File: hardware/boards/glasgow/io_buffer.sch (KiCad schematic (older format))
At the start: 66 parts, among them J2 Conn_02x10_Odd_Even, J6 Conn_01x08, J7 Conn_01x08, U10 DAC081C081CIMK, U11 TPS73101DBV, U16 SN74LVC1T45DCKR, U17 SN74LVC1T45DCKR, U18 SN74LVC1T45DCKR, U19 PCA6408APW, U19 SN74LVC1T45DCKR, U20 SN74LVC1T45DCKR, U21 INA233, U21 SN74LVC1T45DCKR, U5 SN74LVC1T45DCKR, U6 SN74LVC1T45DCKR

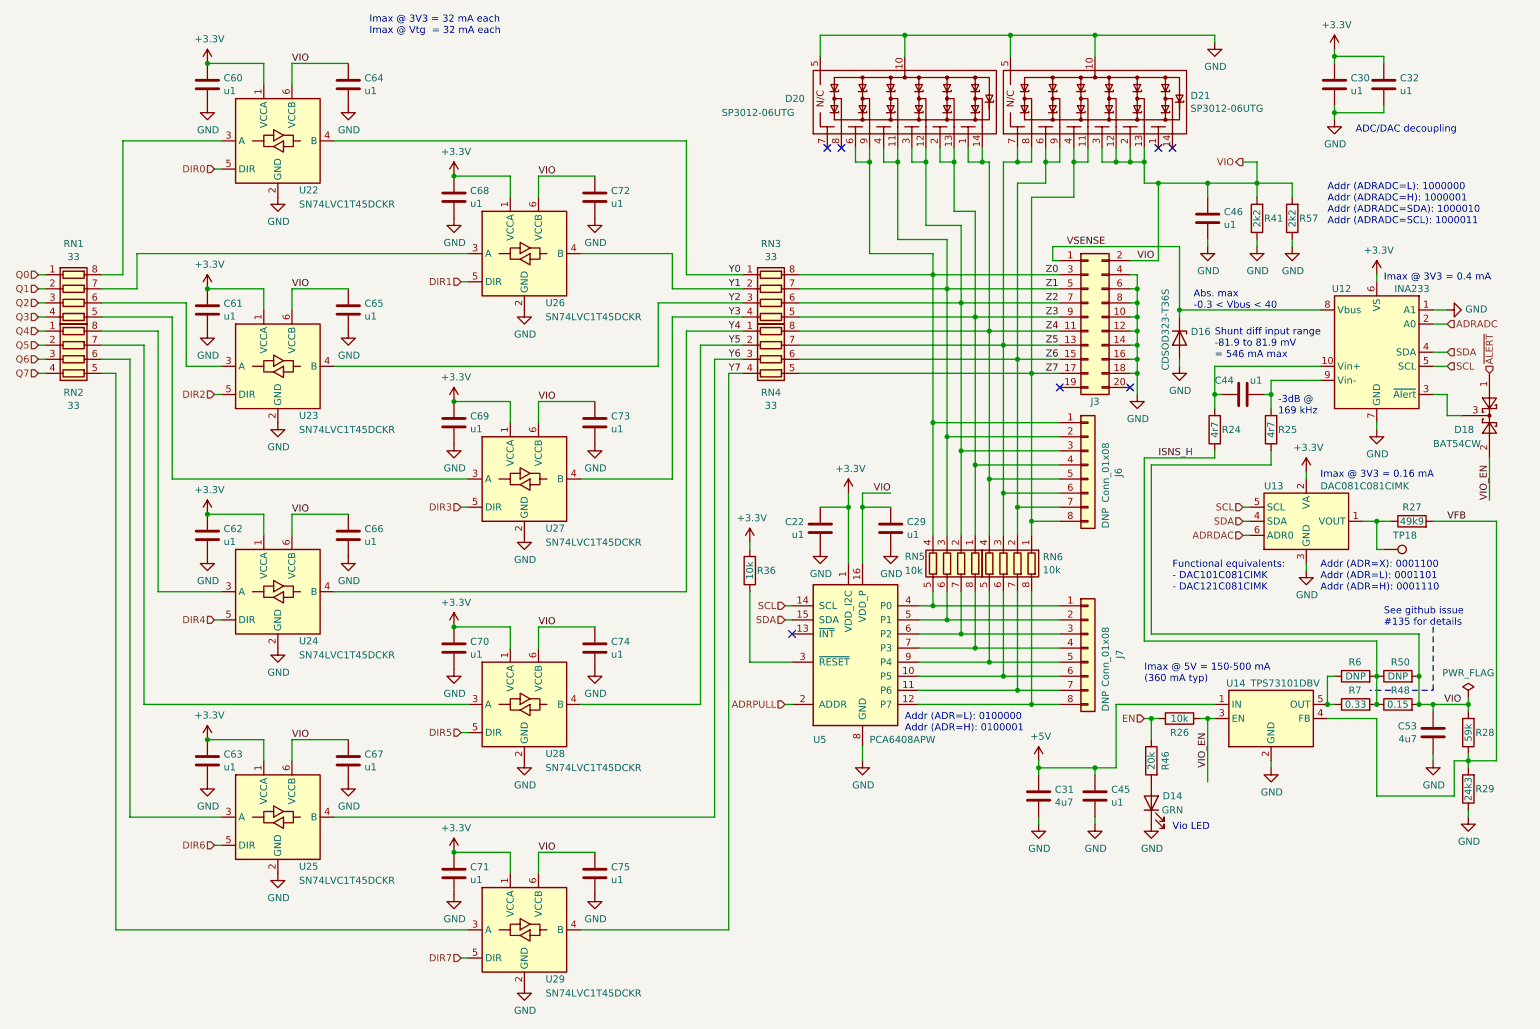
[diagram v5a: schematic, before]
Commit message: revC2: Consolidated sub 1k resistor value notation.
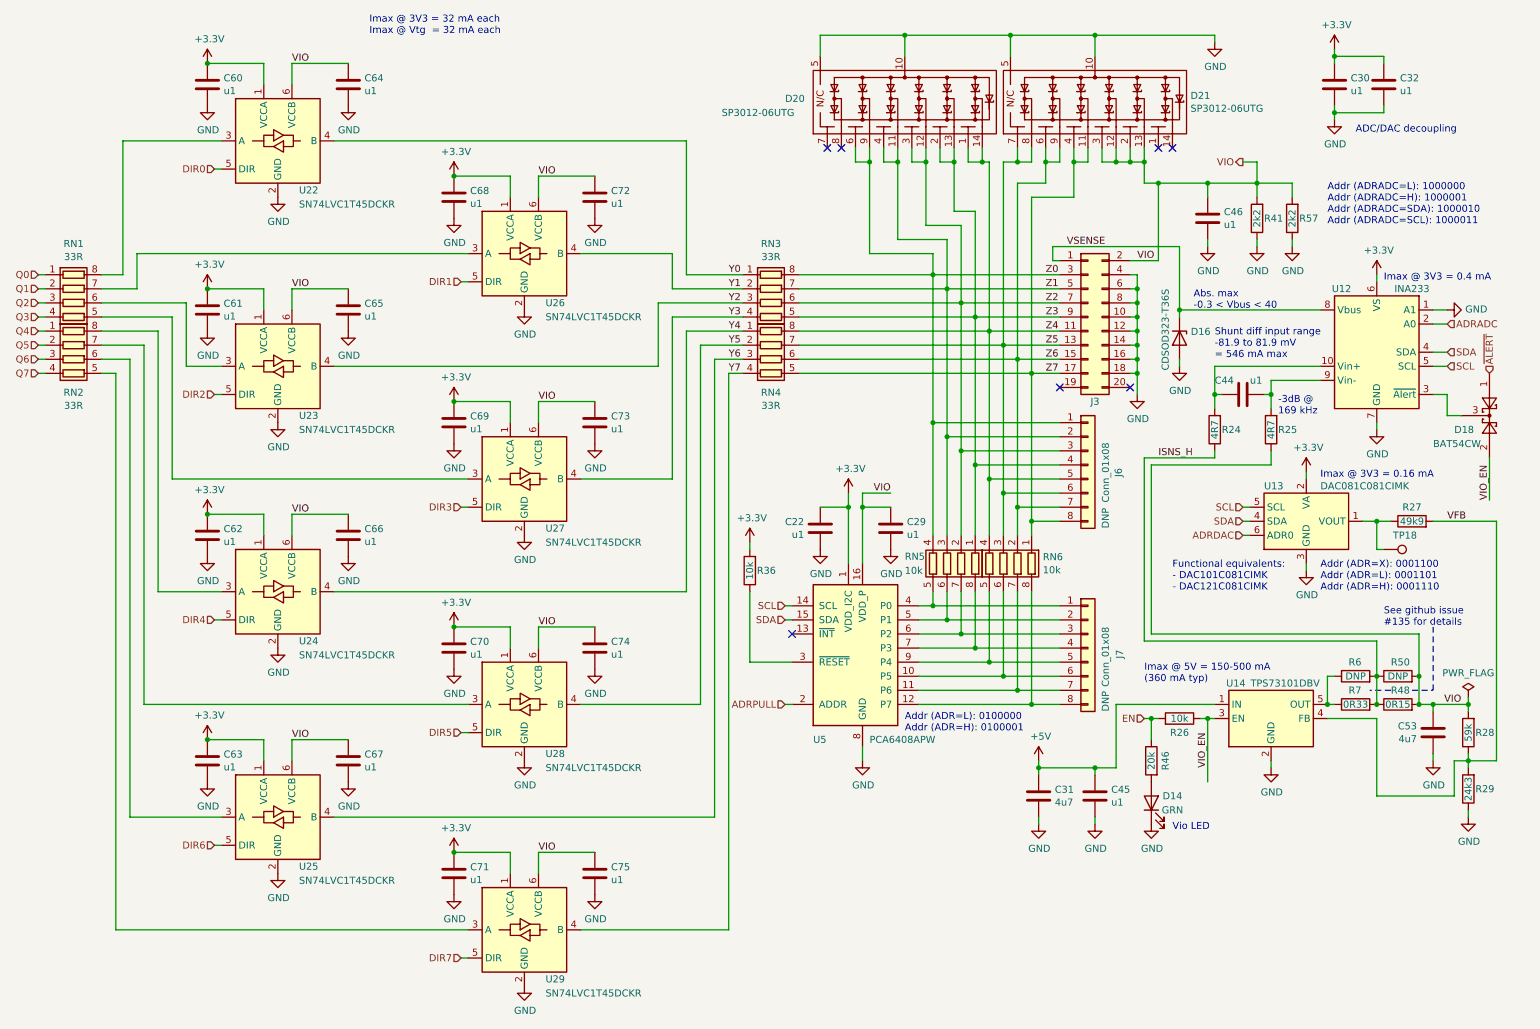
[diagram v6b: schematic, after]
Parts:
- D22, D23: MPN (none) -> SP3012-06UTG; Mfg (none) -> Littlefuse
- R30, R54: value 4r7 -> 4R7; 1b2-bom-key res-0402-4R7 -> res-0402-4r7
- R49: value 0.15 -> 0R15; 1b2-bom-key res-0603-0_15 -> res-0603-0r15
- R56: value 0.33 -> 0R33; 1b2-bom-key res-0603-0_33 -> res-0603-0r33
- RN1, RN2, RN3, RN4: value 33 -> 33R; 1b2-bom-key res-0402cv-array-4-33 -> res-0402cv-array-4-33r; MPN (none) -> YC124-JR-1333RL; Mfg (none) -> Yageo
- RN5, RN6: MPN (none) -> YC124-JR-0710KL; Mfg (none) -> Yageo
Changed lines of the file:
@@
 AR Path="/5C7B59B0/5C9E338E/5CD0C19C" Ref="R48"  Part="1"
 F 0 "R48" V 10550 5500 50  0000 R CNN
-F 1 "0.15" V 10450 5450 50  0000 C CNN
+F 1 "0R15" V 10450 5450 50  0000 C CNN
 F 2 "Resistor_SMD:R_0603_1608Metric" V 10380 5450 50  0001 C CNN
 F 3 "https://www.ohmite.com/assets/docs/res_kdv.pdf" H 10450 5450 50  0001 C CNN
 F 4 "Ohmite" H 4300 500 50  0001 C CNN "Mfg"
 F 5 "KDV06FR150ET" H 4300 500 50  0001 C CNN "MPN"
-F 6 "res-0603-0_15" H 10450 5450 50  0001 C CNN "1b2-bom-key"
+F 6 "res-0603-0r15" H 10450 5450 50  0001 C CNN "1b2-bom-key"
 	1    10450 5450
 	0    -1   -1   0
@@
 AR Path="/5C7B59B0/5C9E337E/5EAC6F23" Ref="RN7"  Part="1"
 F 0 "RN1" V 630 2600 50  0000 C CNN
-F 1 "33" V 723 2600 50  0000 C CNN
+F 1 "33R" V 723 2600 50  0000 C CNN
 F 2 "Glasgow:R_Array_Convex_4x0402" V 1325 2600 50  0001 C CNN
-F 3 "~" H 1050 2600 50  0001 C CNN
-F 4 "res-0402cv-array-4-33" H 1050 2600 50  0001 C CNN "1b2-bom-key"
+F 3 "https://www.mouser.com/datasheet/2/447/PYu-YC_TC_group_51_RoHS_L_7-1313905.pdf" H 1050 2600 50  0001 C CNN
+F 4 "res-0402cv-array-4-33r" H 1050 2600 50  0001 C CNN "1b2-bom-key"
+F 5 "YC124-JR-1333RL" H 1050 2600 50  0001 C CNN "MPN"
+F 6 "Yageo" H 1050 2600 50  0001 C CNN "Mfg"
 	1    1050 2600
 	0    1    1    0
@@
 AR Path="/5C7B59B0/5C9E337E/5EAFC4A6" Ref="RN8"  Part="1"
 F 0 "RN2" V 1286 3000 50  0000 C CNN
-F 1 "33" V 1379 3000 50  0000 C CNN
+F 1 "33R" V 1379 3000 50  0000 C CNN
 F 2 "Glasgow:R_Array_Convex_4x0402" V 1325 3000 50  0001 C CNN
-F 3 "~" H 1050 3000 50  0001 C CNN
-F 4 "res-0402cv-array-4-33" H 1050 3000 50  0001 C CNN "1b2-bom-key"
+F 3 "https://www.mouser.com/datasheet/2/447/PYu-YC_TC_group_51_RoHS_L_7-1313905.pdf" H 1050 3000 50  0001 C CNN
+F 4 "res-0402cv-array-4-33r" H 1050 3000 50  0001 C CNN "1b2-bom-key"
+F 5 "YC124-JR-1333RL" H 1050 3000 50  0001 C CNN "MPN"
+F 6 "Yageo" H 1050 3000 50  0001 C CNN "Mfg"
 	1    1050 3000
 	0    1    1    0
@@
 AR Path="/5C7B59B0/5C9E337E/5EAFCC23" Ref="RN9"  Part="1"
 F 0 "RN3" V 5580 2600 50  0000 C CNN
-F 1 "33" V 5673 2600 50  0000 C CNN
+F 1 "33R" V 5673 2600 50  0000 C CNN
 F 2 "Glasgow:R_Array_Convex_4x0402" V 6275 2600 50  0001 C CNN
-F 3 "~" H 6000 2600 50  0001 C CNN
-F 4 "res-0402cv-array-4-33" H 6000 2600 50  0001 C CNN "1b2-bom-key"
+F 3 "https://www.mouser.com/datasheet/2/447/PYu-YC_TC_group_51_RoHS_L_7-1313905.pdf" H 6000 2600 50  0001 C CNN
+F 4 "res-0402cv-array-4-33r" H 6000 2600 50  0001 C CNN "1b2-bom-key"
+F 5 "YC124-JR-1333RL" H 6000 2600 50  0001 C CNN "MPN"
+F 6 "Yageo" H 6000 2600 50  0001 C CNN "Mfg"
 	1    6000 2600
 	0    1    1    0
@@
 AR Path="/5C7B59B0/5C9E337E/5EB2C386" Ref="RN10"  Part="1"
 F 0 "RN4" V 6236 3000 50  0000 C CNN
-F 1 "33" V 6329 3000 50  0000 C CNN
+F 1 "33R" V 6329 3000 50  0000 C CNN
 F 2 "Glasgow:R_Array_Convex_4x0402" V 6275 3000 50  0001 C CNN
-F 3 "~" H 6000 3000 50  0001 C CNN
-F 4 "res-0402cv-array-4-33" H 6000 3000 50  0001 C CNN "1b2-bom-key"
+F 3 "https://www.mouser.com/datasheet/2/447/PYu-YC_TC_group_51_RoHS_L_7-1313905.pdf" H 6000 3000 50  0001 C CNN
+F 4 "res-0402cv-array-4-33r" H 6000 3000 50  0001 C CNN "1b2-bom-key"
+F 5 "YC124-JR-1333RL" H 6000 3000 50  0001 C CNN "MPN"
+F 6 "Yageo" H 6000 3000 50  0001 C CNN "Mfg"
 	1    6000 3000
 	0    1    1    0
@@
 F 1 "10k" H 7370 4496 50  0000 R CNN
 F 2 "Glasgow:R_Array_Convex_4x0402" V 7925 4450 50  0001 C CNN
-F 3 "~" H 7650 4450 50  0001 C CNN
+F 3 "https://www.mouser.com/datasheet/2/447/PYu-YC_TC_group_51_RoHS_L_7-1313905.pdf" H 7650 4450 50  0001 C CNN
 F 4 "res-0402cv-array-4-10k" H 7650 4450 50  0001 C CNN "1b2-bom-key"
+F 5 "YC124-JR-0710KL" H 7650 4450 50  0001 C CNN "MPN"
+F 6 "Yageo" H 7650 4450 50  0001 C CNN "Mfg"
 	1    7650 4450
 	-1   0    0    1
@@
 F 1 "10k" H 7550 4500 50  0000 R CNN
 F 2 "Glasgow:R_Array_Convex_4x0402" V 7525 4450 50  0001 C CNN
-F 3 "~" H 7250 4450 50  0001 C CNN
+F 3 "https://www.mouser.com/datasheet/2/447/PYu-YC_TC_group_51_RoHS_L_7-1313905.pdf" H 7250 4450 50  0001 C CNN
 F 4 "res-0402cv-array-4-10k" H 7250 4450 50  0001 C CNN "1b2-bom-key"
+F 5 "YC124-JR-0710KL" H 7250 4450 50  0001 C CNN "MPN"
+F 6 "Yageo" H 7250 4450 50  0001 C CNN "Mfg"
 	1    7250 4450
 	-1   0    0    1
@@
 AR Path="/5C7B59B0/5C9E338E/5F1A23B9" Ref="R25"  Part="1"
 F 0 "R25" H 9500 3500 50  0000 R CNN
-F 1 "4r7" V 9550 3500 50  0000 C CNN
+F 1 "4R7" V 9550 3500 50  0000 C CNN
 F 2 "Resistor_SMD:R_0402_1005Metric" V 9480 3500 50  0001 C CNN
 F 3 "https://www.mouser.com/datasheet/2/447/PYu-RC_Group_51_RoHS_L_10-1527934.pdf" H 9550 3500 50  0001 C CNN
 F 4 "Yageo" H 3400 -1450 50  0001 C CNN "Mfg"
 F 5 "RC0402FR-074R7L" H 3400 -1450 50  0001 C CNN "MPN"
-F 6 "res-0402-4R7" H 9550 3500 50  0001 C CNN "1b2-bom-key"
+F 6 "res-0402-4r7" H 9550 3500 50  0001 C CNN "1b2-bom-key"
 	1    9550 3500
 	-1   0    0    1
@@
 AR Path="/5C7B59B0/5C9E338E/5F1A3005" Ref="R24"  Part="1"
 F 0 "R24" H 9100 3500 50  0000 R CNN
-F 1 "4r7" V 9150 3500 50  0000 C CNN
+F 1 "4R7" V 9150 3500 50  0000 C CNN
 F 2 "Resistor_SMD:R_0402_1005Metric" V 9080 3500 50  0001 C CNN
 F 3 "https://www.mouser.com/datasheet/2/447/PYu-RC_Group_51_RoHS_L_10-1527934.pdf" H 9150 3500 50  0001 C CNN
 F 4 "Yageo" H 3000 -1450 50  0001 C CNN "Mfg"
 F 5 "RC0402FR-074R7L" H 3000 -1450 50  0001 C CNN "MPN"
-F 6 "res-0402-4R7" H 9150 3500 50  0001 C CNN "1b2-bom-key"
+F 6 "res-0402-4r7" H 9150 3500 50  0001 C CNN "1b2-bom-key"
 	1    9150 3500
 	-1   0    0    1
@@
 F 3 "https://www.littelfuse.com/~/media/electronics/datasheets/tvs_diode_arrays/littelfuse_tvs_diode_array_sp3012_datasheet.pdf.pdf" H 8625 1175 50  0001 C CNN
 F 4 "diode-14udfn-sp3012-06utg" H 8300 1150 50  0001 C CNN "1b2-bom-key"
+F 5 "SP3012-06UTG" H 8300 1150 50  0001 C CNN "MPN"
+F 6 "Littlefuse" H 8300 1150 50  0001 C CNN "Mfg"
 	1    8300 1150
 	-1   0    0    1
@@
 F 3 "https://www.littelfuse.com/~/media/electronics/datasheets/tvs_diode_arrays/littelfuse_tvs_diode_array_sp3012_datasheet.pdf.pdf" H 7275 1175 50  0001 C CNN
 F 4 "diode-14udfn-sp3012-06utg" H 6950 1150 50  0001 C CNN "1b2-bom-key"
+F 5 "SP3012-06UTG" H 6950 1150 50  0001 C CNN "MPN"
+F 6 "Littlefuse" H 6950 1150 50  0001 C CNN "Mfg"
 	1    6950 1150
 	-1   0    0    1
@@
 AR Path="/5C7B59B0/5C9E338E/5F25DFB3" Ref="R7"  Part="1"
 F 0 "R7" V 10250 5500 50  0000 R CNN
-F 1 "0.33" V 10150 5450 50  0000 C CNN
+F 1 "0R33" V 10150 5450 50  0000 C CNN
 F 2 "Resistor_SMD:R_0603_1608Metric" V 10080 5450 50  0001 C CNN
 F 3 "https://www.ohmite.com/assets/docs/res_kdv.pdf" H 10150 5450 50  0001 C CNN
 F 4 "Ohmite" H 4000 500 50  0001 C CNN "Mfg"
 F 5 "KDV06FR330ET" H 4000 500 50  0001 C CNN "MPN"
-F 6 "res-0603-0_33" H 10150 5450 50  0001 C CNN "1b2-bom-key"
+F 6 "res-0603-0r33" H 10150 5450 50  0001 C CNN "1b2-bom-key"
 	1    10150 5450
 	0    -1   -1   0

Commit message: revC2: add rc filter for Vsense input
The capacitor is currently DNP as it is currently unknown if the filter is necessary.
The resistor is the lowest value in the BOM (4r7).
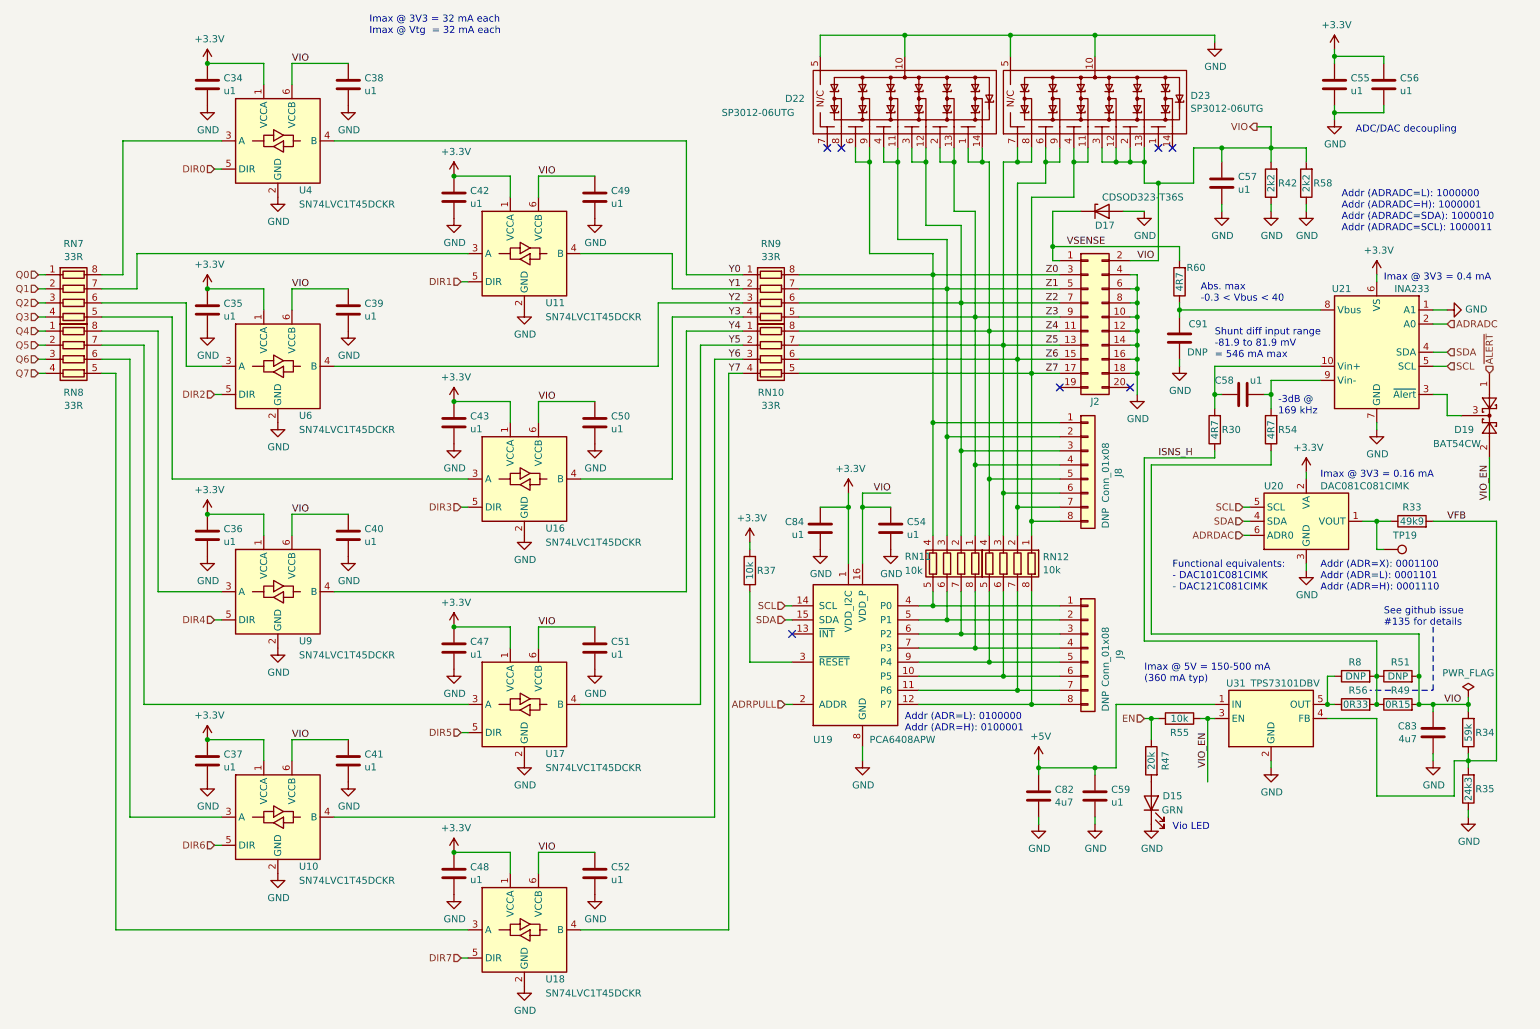
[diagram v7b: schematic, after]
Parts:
- added C91: DNP, Capacitor_SMD:C_0402_1005Metric, symbol Device:C
- added R60: 4R7, Resistor_SMD:R_0402_1005Metric, symbol Device:R
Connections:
- net GND: now also C91.1
- net VSENSE: now also R60.2; no longer U21.8 (Vbus)
- new net: C91.2, R60.1, U21.8 (Vbus)
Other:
- moved on the sheet: C57, D17, R42, R58

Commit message: revC2: Fix ESD protection footprint & clean up routing
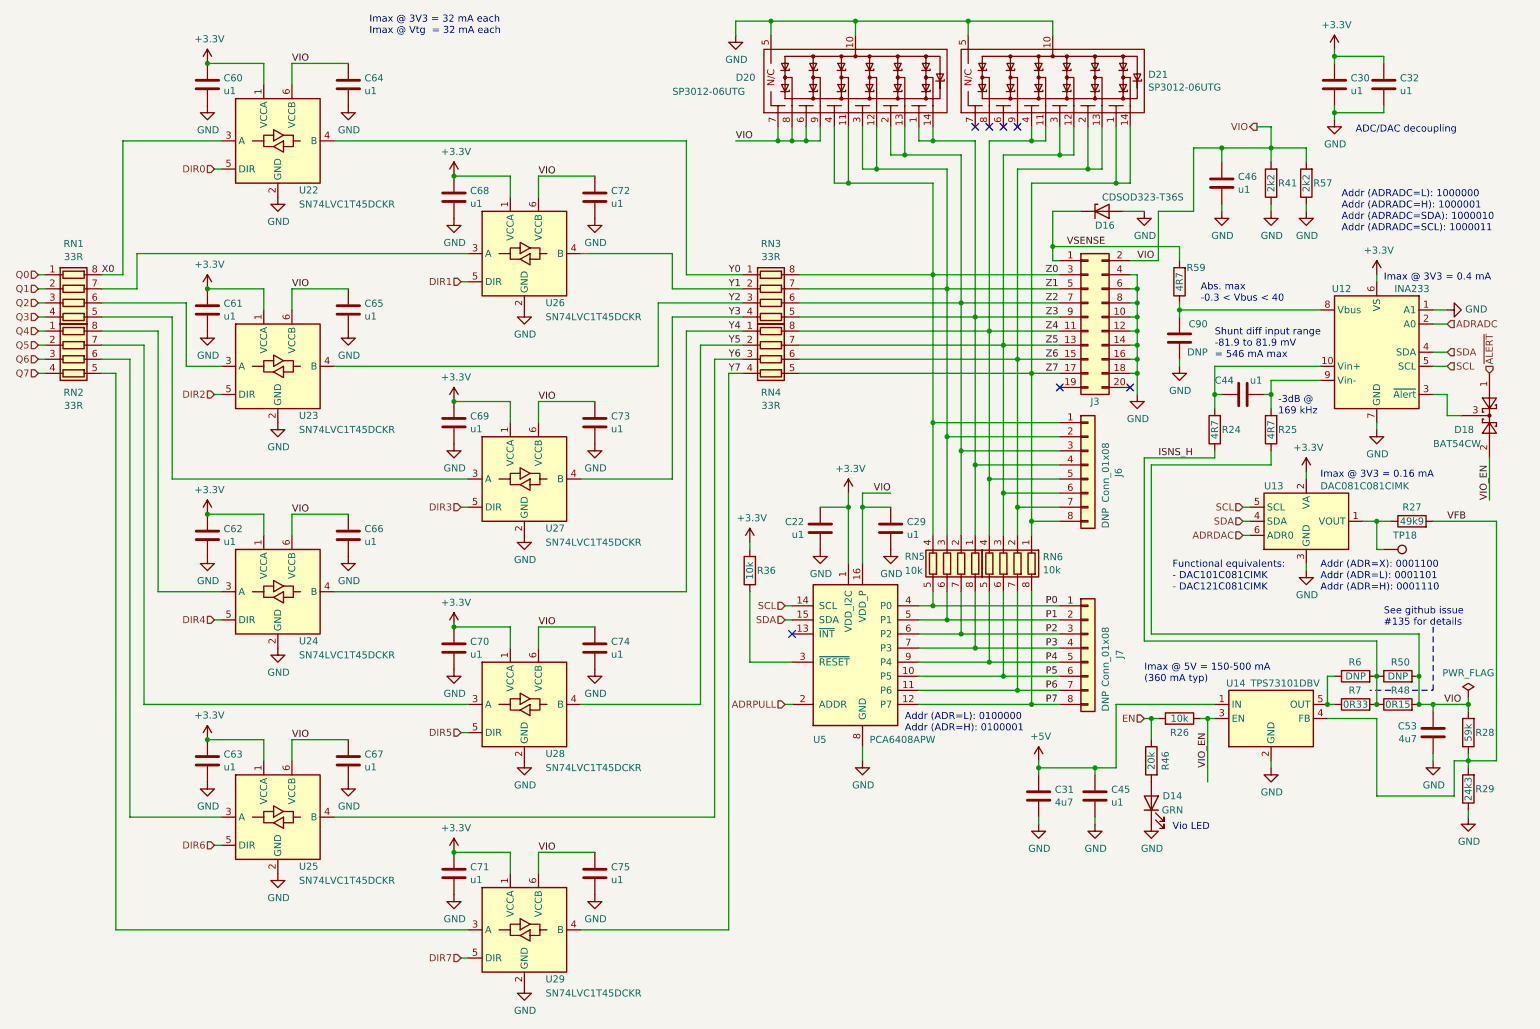
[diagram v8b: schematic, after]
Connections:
- net VIO: now also D22.6 (N/C), D22.7 (N/C), D22.8 (Ch6), D22.9 (Ch5); no longer D23.12 (Ch3), D23.13 (Ch2), D23.2 (N/C), D23.3 (N/C)
- net Z0: now also D22.11 (Ch4), D22.4 (N/C); no longer D22.6 (N/C), D22.9 (Ch5)
- net Z1: now also D22.12 (Ch3), D22.3 (N/C); no longer D22.11 (Ch4), D22.4 (N/C)
- net Z2: now also D22.13 (Ch2), D22.2 (N/C); no longer D22.12 (Ch3), D22.3 (N/C)
- net Z3: now also D22.1 (N/C), D22.14 (Ch1); no longer D22.13 (Ch2), D22.2 (N/C)
- net Z4: now also D23.11 (Ch4), D23.4 (N/C); no longer D22.1 (N/C), D22.14 (Ch1)
- net Z5: now also D23.12 (Ch3), D23.3 (N/C); no longer D23.7 (N/C), D23.8 (Ch6)
- net Z6: now also D23.13 (Ch2), D23.2 (N/C); no longer D23.6 (N/C), D23.9 (Ch5)
- net Z7: now also D23.1 (N/C), D23.14 (Ch1); no longer D23.11 (Ch4), D23.4 (N/C)
- net X0: now reaches RN1.8 (R1.2), U5.3 (A)
- net P5: now reaches J7.6 (Pin_6), RN6.6 (R3.2), U19.10 (P5)
- net P6: now reaches J7.7 (Pin_7), RN6.7 (R2.2), U19.11 (P6)
- net P7: now reaches J7.8 (Pin_8), RN6.8 (R1.2), U19.12 (P7)
- net P0: now reaches J7.1 (Pin_1), RN5.5 (R4.2), U19.4 (P0)
- net P1: now reaches J7.2 (Pin_2), RN5.6 (R3.2), U19.5 (P1)
- net P2: now reaches J7.3 (Pin_3), RN5.7 (R2.2), U19.6 (P2)
- net P3: now reaches J7.4 (Pin_4), RN5.8 (R1.2), U19.7 (P3)
- net P4: now reaches J7.5 (Pin_5), RN6.5 (R4.2), U19.9 (P4)
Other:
- moved on the sheet: D20, D21
